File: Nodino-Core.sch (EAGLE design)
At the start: 15 parts, among them CON1 NODINO-JTAGMODULE, CON2 USB-OTG_SHIELD, IC1 STM32F373CCT6, IC2 AP733333SAG, Q1 16MHz, Q2 32.768kHz

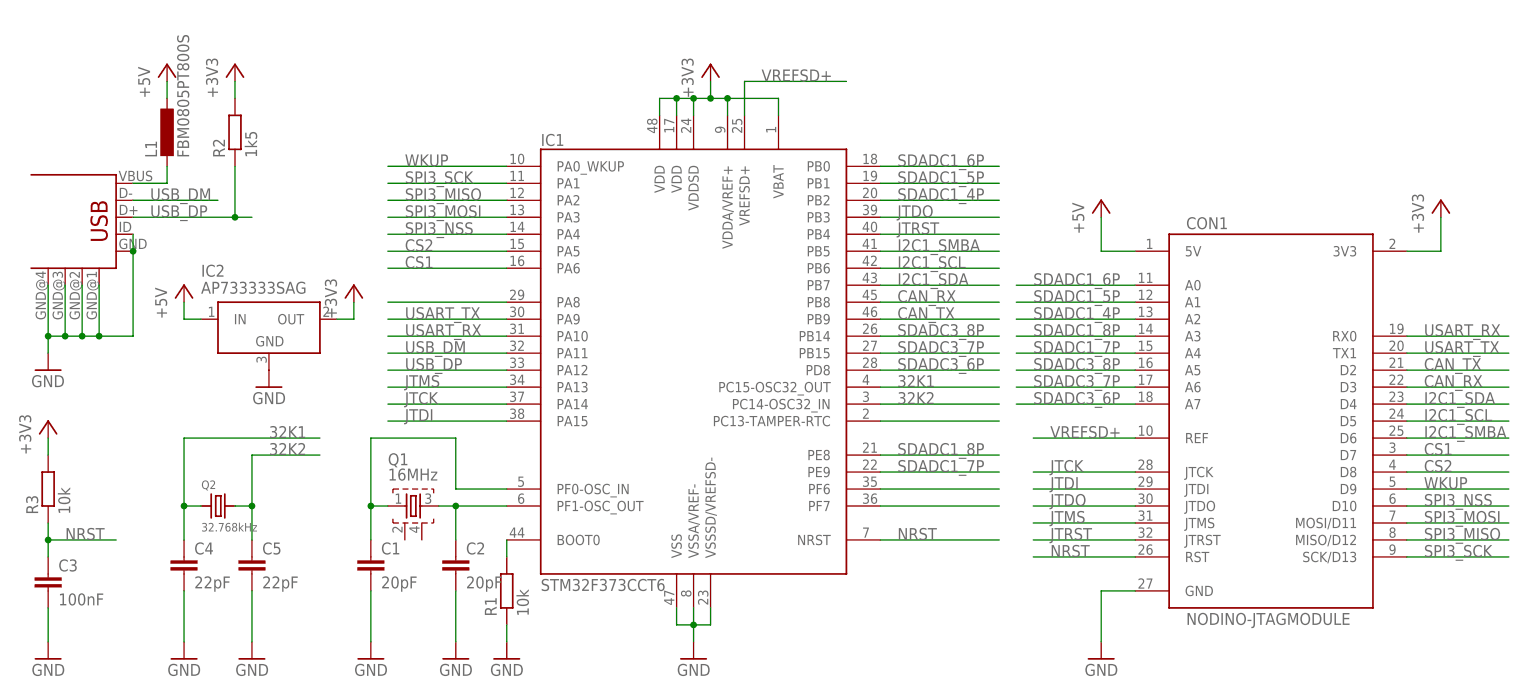
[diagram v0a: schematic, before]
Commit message: added filter capacitors
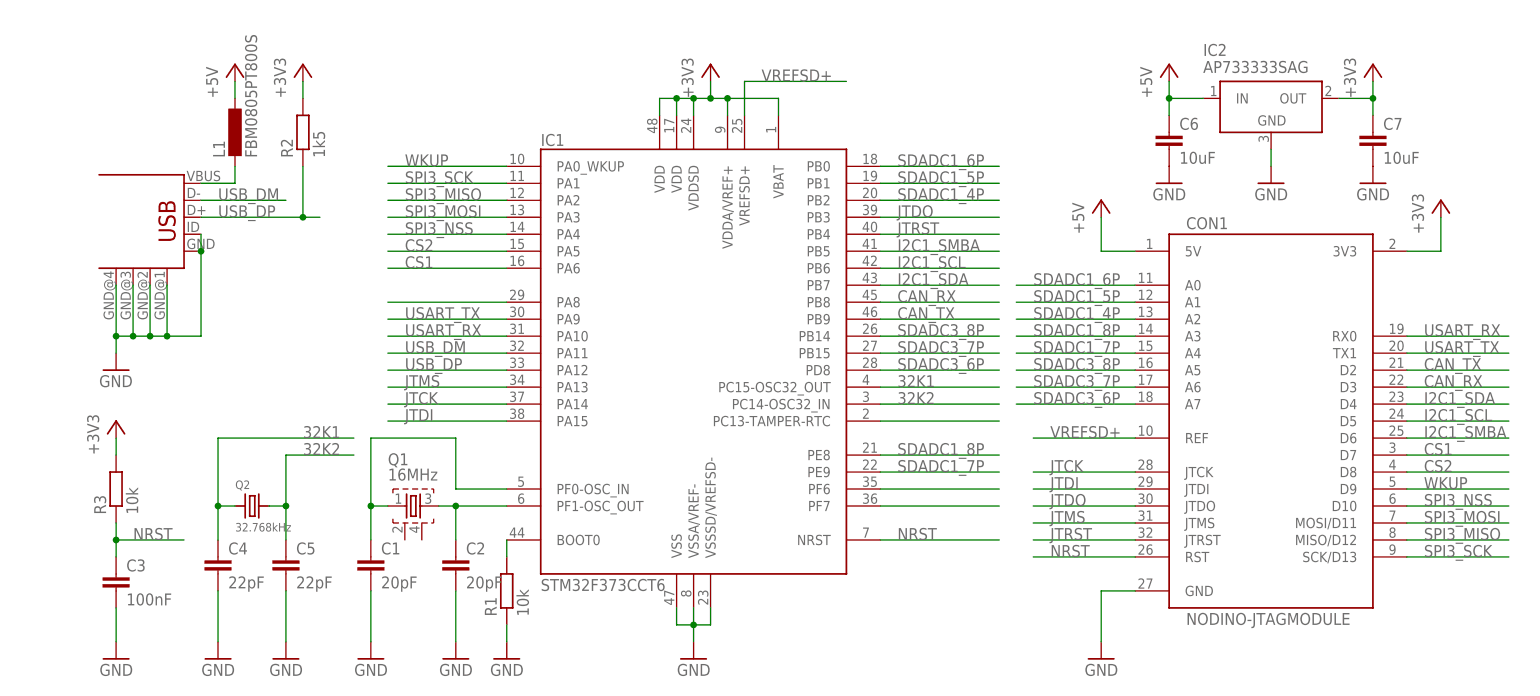
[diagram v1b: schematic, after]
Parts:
- added C6, C7: 10uF, resistor:C-EUC0603K
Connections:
- net +3V3: now also C7.1
- net +5V: now also C6.1
- net GND: now also C6.2, C7.2
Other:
- moved on the sheet: C3, C4, C5, IC2, L1, Q2, R2, R3
